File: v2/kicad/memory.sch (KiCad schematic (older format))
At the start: 3 parts, among them U10 74AC138, U4 IS61C1024AL-12KLI, U9 74AC139

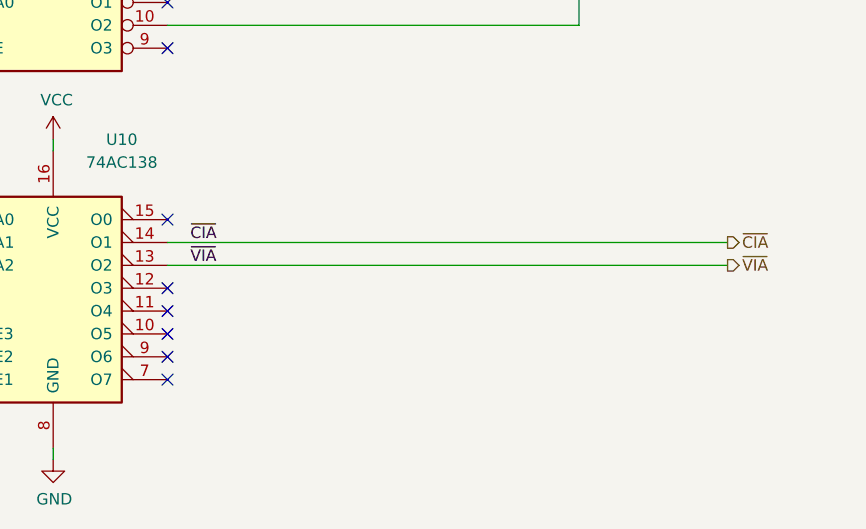
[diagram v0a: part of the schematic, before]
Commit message: new revision - dual 6526
new revision - dual 6526
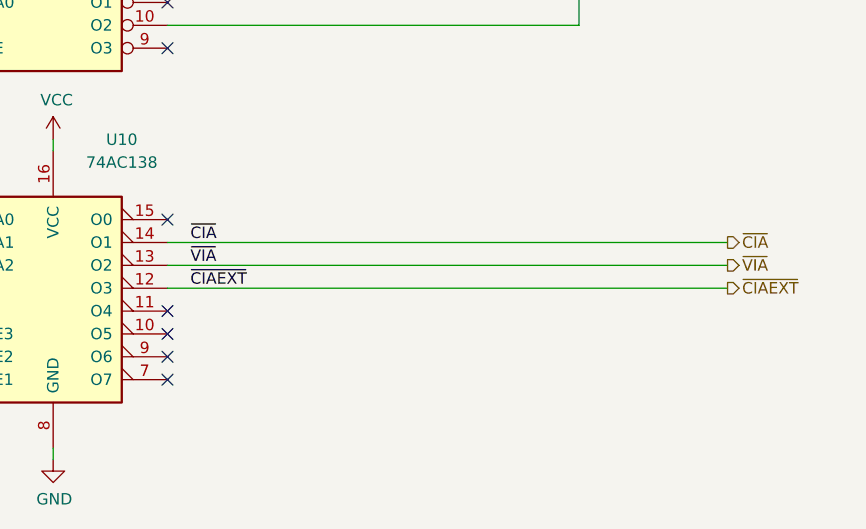
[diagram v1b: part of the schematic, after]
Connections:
- net ~CIAEXT: now reaches U10.12 (O3)
- no-connect marks 12 -> 11
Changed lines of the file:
@@
 NoConn ~ 6600 2400
 NoConn ~ 6600 5800
-NoConn ~ 6600 6100
 NoConn ~ 6600 6200
 NoConn ~ 6600 6300
@@
 Wire Wire Line
 	6100 6800 6100 6850
+Text Label 6700 1500 0    50   ~ 0
+D5
+Text Label 6700 1700 0    50   ~ 0
+D7
+Wire Wire Line
+	6600 6100 9050 6100
+Text HLabel 9050 6100 2    50   Output ~ 0
+~CIAEXT
 Wire Bus Line
 	7100 700  7100 2100
 Wire Bus Line
 	5200 800  5200 6300
-Text Label 6700 1500 0    50   ~ 0
-D5
-Text Label 6700 1700 0    50   ~ 0
-D7
+Text Label 6700 6100 0    50   ~ 0
+~CIAEXT
 $EndSCHEMATC
